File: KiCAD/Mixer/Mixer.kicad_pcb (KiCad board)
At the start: 2 copper layers, 30 x 118.5 mm, 63 parts, among them J1 AudioJack2, J2 Conn_02x05_Odd_Even, J3 Conn_02x03_Odd_Even, J4 Conn_02x08_Odd_Even, J5 AudioJack2, Q1 MMBFJ111, Q2 MMBFJ111, Q3 MMBFJ111, Q4 MMBFJ111, SW1 SW_MEC_5G, SW2 SW_MEC_5G, U1 NE5532, U2 NE5532, U3 NE5532, U4 NE5532, U5 NE5532, U6 NE5532

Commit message: überarbeitete Schaltung und PCB Desing...v1.0 FERTIG
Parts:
- removed C2: 100n, Capacitor_SMD:C_0805_2012Metric_Pad1.18x1.45mm_HandSolder
- removed D1, D2, D5, D6: D, Diode_SMD:D_SOD-123
- removed J2: Conn_02x05_Odd_Even, Connector_PinHeader_2.54mm:PinHeader_2x05_P2.54mm_Vertical
- removed J3: Conn_02x03_Odd_Even, Connector_PinHeader_2.54mm:PinHeader_2x03_P2.54mm_Vertical
- removed RV8: 100, Potentiometer_THT:Potentiometer_Alps_RK09K_Single_Vertical
- added C11: 100n, Capacitor_SMD:C_0805_2012Metric_Pad1.18x1.45mm_HandSolder, B.Cu at (146.3, 55.4)
- added C12: 100n, Capacitor_SMD:C_0805_2012Metric_Pad1.18x1.45mm_HandSolder, B.Cu at (146.3, 65.0)
- added C13: 100n, Capacitor_SMD:C_0805_2012Metric_Pad1.18x1.45mm_HandSolder, B.Cu at (130.9, 62.9)
- added C14: 100n, Capacitor_SMD:C_0805_2012Metric_Pad1.18x1.45mm_HandSolder, B.Cu at (130.9, 72.6)
- added C15: 100n, Capacitor_SMD:C_0805_2012Metric_Pad1.18x1.45mm_HandSolder, B.Cu at (146.3, 63.0)
- added C16: 100n, Capacitor_SMD:C_0805_2012Metric_Pad1.18x1.45mm_HandSolder, B.Cu at (146.3, 72.6)
- added C17: 100u, Capacitor_THT:CP_Radial_D5.0mm_P2.50mm, B.Cu at (138.6, 125.4)
- added C33: 100n, Capacitor_SMD:C_0805_2012Metric_Pad1.18x1.45mm_HandSolder, B.Cu at (129.7, 47.6)
- added C34: 100n, Capacitor_SMD:C_0805_2012Metric_Pad1.18x1.45mm_HandSolder, B.Cu at (139.7, 47.7)
- added C35: 100n, Capacitor_SMD:C_0805_2012Metric_Pad1.18x1.45mm_HandSolder, B.Cu at (137.5, 47.6)
- added C37: 100n, Capacitor_SMD:C_0805_2012Metric_Pad1.18x1.45mm_HandSolder, B.Cu at (147.3, 47.6)
- added C40: 100n, Capacitor_SMD:C_0805_2012Metric_Pad1.18x1.45mm_HandSolder, B.Cu at (138.8, 85.2)
- added C41: 100n, Capacitor_SMD:C_0805_2012Metric_Pad1.18x1.45mm_HandSolder, B.Cu at (138.8, 94.9)
- added D3: 1N5711, Diode_SMD:D_SMA, B.Cu at (133.5, 126.9)
- added D4: 1N5711, Diode_SMD:D_SMA, B.Cu at (143.7, 137.1)
- added J10: Conn_02x09_Odd_Even, Connector_PinHeader_2.54mm:PinHeader_2x09_P2.54mm_Vertical, B.Cu at (143.3, 99.0)
- added J11: Conn_02x09_Odd_Even, Connector_PinHeader_2.54mm:PinHeader_2x09_P2.54mm_Vertical, B.Cu at (136.4, 99.0)
- added J6: Conn_02x05_Odd_Even, Connector_PinHeader_2.54mm:PinHeader_2x05_P2.54mm_Vertical, B.Cu at (139.8, 128.9)
- added J7: Conn_01x02_Socket, Connector_PinHeader_2.54mm:PinHeader_1x02_P2.54mm_Vertical, F.Cu at (146.0, 33.6)
- added J8: Conn_01x02_Socket, Connector_PinHeader_2.54mm:PinHeader_1x02_P2.54mm_Vertical, F.Cu at (135.3, 37.4)
- added J9: Conn_01x02_Socket, Connector_PinHeader_2.54mm:PinHeader_1x02_P2.54mm_Vertical, F.Cu at (146.0, 37.3)
- added R25: 1k, Resistor_SMD:R_0805_2012Metric_Pad1.20x1.40mm_HandSolder, B.Cu at (151.1, 59.3)
- added R26: 1k, Resistor_SMD:R_0805_2012Metric_Pad1.20x1.40mm_HandSolder, B.Cu at (141.6, 59.2)
- added R29: 1k, Resistor_SMD:R_0805_2012Metric_Pad1.20x1.40mm_HandSolder, B.Cu at (143.5, 80.2)
- added R30: 1k, Resistor_SMD:R_0805_2012Metric_Pad1.20x1.40mm_HandSolder, B.Cu at (134.0, 80.2)
- added R31: 1k, Resistor_SMD:R_0805_2012Metric_Pad1.20x1.40mm_HandSolder, B.Cu at (132.0, 84.0)
- added R32: 1k, Resistor_SMD:R_0805_2012Metric_Pad1.20x1.40mm_HandSolder, B.Cu at (132.0, 80.2)
- added R33: 1k, Resistor_SMD:R_0805_2012Metric_Pad1.20x1.40mm_HandSolder, B.Cu at (145.5, 80.2)
- added R34: 1k, Resistor_SMD:R_0805_2012Metric_Pad1.20x1.40mm_HandSolder, B.Cu at (145.5, 84.0)
- added R35: 1k, Resistor_SMD:R_0805_2012Metric_Pad1.20x1.40mm_HandSolder, B.Cu at (143.5, 84.0)
- added R36: 1k, Resistor_SMD:R_0805_2012Metric_Pad1.20x1.40mm_HandSolder, B.Cu at (134.0, 84.0)
- added R37: 1k, Resistor_SMD:R_0805_2012Metric_Pad1.20x1.40mm_HandSolder, B.Cu at (143.6, 91.2)
- added R38: 1k, Resistor_SMD:R_0805_2012Metric_Pad1.20x1.40mm_HandSolder, B.Cu at (134.0, 91.0)
- added R39: 1k, Resistor_SMD:R_0805_2012Metric_Pad1.20x1.40mm_HandSolder, B.Cu at (124.1, 59.2)
- added R40: 1k, Resistor_SMD:R_0805_2012Metric_Pad1.20x1.40mm_HandSolder, B.Cu at (139.6, 59.2)
- added R41: 1k, Resistor_SMD:R_0805_2012Metric_Pad1.20x1.40mm_HandSolder, B.Cu at (132.0, 91.0)
- added R42: 1k, Resistor_SMD:R_0805_2012Metric_Pad1.20x1.40mm_HandSolder, B.Cu at (145.6, 91.2)
- added R43: 1k, Resistor_SMD:R_0805_2012Metric_Pad1.20x1.40mm_HandSolder, B.Cu at (137.6, 59.2)
- added R44: 1k, Resistor_SMD:R_0805_2012Metric_Pad1.20x1.40mm_HandSolder, B.Cu at (153.1, 59.3)
- added R45: 1k, Resistor_SMD:R_0805_2012Metric_Pad1.20x1.40mm_HandSolder, B.Cu at (139.6, 68.8)
- added R46: 1k, Resistor_SMD:R_0805_2012Metric_Pad1.20x1.40mm_HandSolder, B.Cu at (153.1, 68.9)
- added R47: 1k, Resistor_SMD:R_0805_2012Metric_Pad1.20x1.40mm_HandSolder, B.Cu at (151.1, 68.9)
- added R48: 1k, Resistor_SMD:R_0805_2012Metric_Pad1.20x1.40mm_HandSolder, B.Cu at (141.6, 68.8)
- added R49: 1k, Resistor_SMD:R_0805_2012Metric_Pad1.20x1.40mm_HandSolder, B.Cu at (124.1, 68.8)
- added R50: 1k, Resistor_SMD:R_0805_2012Metric_Pad1.20x1.40mm_HandSolder, B.Cu at (137.6, 68.8)
- added R51: 1k, Resistor_SMD:R_0805_2012Metric_Pad1.20x1.40mm_HandSolder, B.Cu at (135.6, 68.8)
- added R52: 1k, Resistor_SMD:R_0805_2012Metric_Pad1.20x1.40mm_HandSolder, B.Cu at (126.1, 68.8)
- added RV10: 1k, Potentiometer_THT:Potentiometer_Alps_RK09K_Single_Vertical, F.Cu at (118.4, 87.4)
- added RV11: 1k, Potentiometer_THT:Potentiometer_Alps_RK09K_Single_Vertical, F.Cu at (153.7, 71.8)
- added RV12: 1k, Potentiometer_THT:Potentiometer_Alps_RK09K_Single_Vertical, F.Cu at (153.7, 87.4)
- added U7: NE5532, Package_SO:SOIC-8_3.9x4.9mm_P1.27mm, B.Cu at (146.3, 59.2)
- added U8: NE5532, Package_SO:SOIC-8_3.9x4.9mm_P1.27mm, B.Cu at (146.3, 68.8)
- C1, C3: value 470u -> 4,7
- C4, C6: value 100n -> 220n
- C5: value 100n -> 100u; footprint Capacitor_SMD:C_0805_2012Metric_Pad1.18x1.45mm_HandSolder -> Capacitor_THT:CP_Radial_D5.0mm_P2.50mm
- J4: value Conn_02x08_Odd_Even -> Conn_01x02_Socket; footprint Connector_PinHeader_2.54mm:PinHeader_2x08_P2.54mm_Vertical -> Connector_PinHeader_2.54mm:PinHeader_1x02_P2.54mm_Vertical; moved to F.Cu
- R1, R13, R15, R3: value R -> 10k
- R11, R12: value 100 -> R
- R14, R2: value R -> 1k
- R23, R24, RV4: value 100 -> 1k
- moved C5 171.1 mm to (138.6, 145.0), turned to 90 degrees
- moved R12 147.1 mm to (160.4, 38.5), turned to -90 degrees
- moved R13 134.5 mm to (159.8, 57.8)
- moved R18 134.2 mm to (155.9, 129.9), turned to 180 degrees
- moved R16 133.7 mm to (155.9, 131.9), turned to 0 degrees
- moved J4 133.7 mm to (135.3, 33.6), turned to -90 degrees
- moved C3 132.9 mm to (162.5, 38.5), turned to -90 degrees
- moved R21 132.8 mm to (157.2, 100.4), turned to 0 degrees
- moved R22 132.6 mm to (157.2, 107.1), turned to 0 degrees
- moved J5 131.9 mm to (151.1, 35.5)
- moved R19 131.8 mm to (155.9, 127.9), turned to 0 degrees
- moved C9 131.5 mm to (138.7, 77.6), turned to 180 degrees
- moved RV7 131.4 mm to (153.7, 105.0)
- moved R17 130.4 mm to (155.9, 125.8), turned to 180 degrees
- moved SW2 130.4 mm to (159.4, 124.4)
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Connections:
- C10 pad 2: +12V -> /Channel/+12V
- C5 pad 2: +12V -> Net-(D4-K)
- C7 pad 2: +12V -> /Channel/+12V
- C8 pad 2: +12V -> /Channel/+12V
- C9 pad 2: +12V -> /Channel/+12V
- J4 pad 1: -12V -> Net-(J4-Pin_1)
- J4 pad 2: -12V -> /Channel/Gain/gain_out
- R1 pad 1: Net-(D1-K) -> Net-(J4-Pin_1)
- R10 pad 2: /Channel/Main Mix/main_inR -> /Channel/Ch1_outR
- R11 pad 1: /Channel/Main Mix/main_inL -> GND
- R11 pad 2: Net-(U3A-+) -> /Channel/Gain/gain_in
- R12 pad 1: /Channel/Main Mix/main_inR -> GND
- R12 pad 2: Net-(U3B-+) -> /Channel/Gain1/gain_in
- R2 pad 2: Net-(D1-K) -> Net-(J4-Pin_1)
- R21 pad 2: /Channel/Main Mix1/main_inL -> /Channel/Ch2_outL
- R22 pad 2: /Channel/Main Mix1/main_inR -> /Channel/Ch2_outR
- R23 pad 1: /Channel/Main Mix1/main_inL -> Net-(U3B--)
- R23 pad 2: Net-(U5A-+) -> Net-(R23-Pad2)
- R24 pad 1: /Channel/Main Mix1/main_inR -> Net-(U3A--)
- R24 pad 2: Net-(U5B-+) -> Net-(R24-Pad2)
- R9 pad 2: /Channel/Main Mix/main_inL -> /Channel/Ch1_outL
- RV4 pad 1: Net-(U3A--) -> /Channel/Ch1_outL
- RV4 pad 2: /Channel/ch1send_L -> Net-(U3A--)
- RV4 pad 3: /Channel/ch1send_L -> Net-(U3A--)
- SW1 pad 1: -12V -> /Channel/-12V
- SW1 pad 2: -12V -> /Channel/-12V
- SW2 pad 1: -12V -> /Channel/-12V
- SW2 pad 2: -12V -> /Channel/-12V
- U1 pad 2: Net-(D1-K) -> Net-(J4-Pin_1)
- U1 pad 4: -12V -> /Channel/-12V
- U1 pad 8: +12V -> /Channel/+12V
- U2 pad 4: -12V -> /Channel/-12V
- U2 pad 8: +12V -> /Channel/+12V
- U3 pad 1: /Channel/ch1send_L -> Net-(R24-Pad2)
- U3 pad 3: Net-(U3A-+) -> GND
- U3 pad 4: -12V -> /Channel/-12V
- U3 pad 5: Net-(U3B-+) -> GND
- U3 pad 7: /Channel/ch1send_R -> Net-(R23-Pad2)
- U3 pad 8: +12V -> /Channel/+12V
- U4 pad 1: /Channel/ch1out_L -> Net-(R29-Pad2)
- U4 pad 2: /Channel/ch1out_L -> Net-(U4A--)
- U4 pad 3: /Channel/Main Mix/main_inL -> GND
- U4 pad 4: -12V -> /Channel/-12V
- U4 pad 5: /Channel/Main Mix/main_inR -> GND
- U4 pad 6: /Channel/ch1out_R -> Net-(U4B--)
- U4 pad 7: /Channel/ch1out_R -> Net-(R30-Pad2)
- U4 pad 8: +12V -> /Channel/+12V
- U5 pad 1: /Channel/ch1send_L -> /Channel/main_mixL
- U5 pad 3: Net-(U5A-+) -> GND
- U5 pad 4: -12V -> /Channel/-12V
- U5 pad 5: Net-(U5B-+) -> GND
- U5 pad 7: /Channel/ch1send_R -> /Channel/main_mixR
- U5 pad 8: +12V -> /Channel/+12V
- U6 pad 1: /Channel/ch1out_L -> /Channel/send_out1L
- U6 pad 2: /Channel/ch1out_L -> Net-(U6A--)
- U6 pad 3: /Channel/Main Mix1/main_inL -> GND
- U6 pad 4: -12V -> /Channel/-12V
- U6 pad 5: /Channel/Main Mix1/main_inR -> GND
- U6 pad 6: /Channel/ch1out_R -> Net-(U6B--)
- U6 pad 7: /Channel/ch1out_R -> /Channel/send_out1R
- U6 pad 8: +12V -> /Channel/+12V
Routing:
- net /Channel/-12V: track 0.00 -> 224.4 mm, vias 0 -> 10
- net /Channel/+12V: track 0.00 -> 143.8 mm, vias 0 -> 9
- net /Channel/Gain1/gain_out: track 0.00 -> 112.7 mm, vias 0 -> 2
- net /Channel/Gain/gain_out: track 0.00 -> 112.2 mm, vias 0 -> 5
- net /Channel/Fader/fader_out: track 0.00 -> 109.7 mm, vias 0 -> 1
- net GND: track 0.00 -> 104.5 mm, vias 0 -> 160
- net /Channel/Fader1/fader_out: track 0.00 -> 101.5 mm, vias 0 -> 1
- net /Channel/Ch1_outL: track 0.00 -> 80.1 mm, vias 0 -> 4
- net Net-(U1B--): track 0.00 -> 79.8 mm, vias 0 -> 2
- net Net-(U2B--): track 0.00 -> 78.0 mm, vias 0 -> 2
- net /Channel/pre_send2L: track 0.00 -> 75.8 mm, vias 0 -> 3
- net /Channel/pre_send2R: track 0.00 -> 72.3 mm, vias 0 -> 4
- net /Channel/pre_send1R: track 0.00 -> 68.0 mm, vias 0 -> 1
- net /Channel/Ch2_outL: track 0.00 -> 64.0 mm
- net /Channel/send_out2R: track 0.00 -> 62.1 mm, vias 0 -> 4
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- added copper zone on B.Cu, net GND
- added copper zone on F.Cu, net GND
- added copper zone on In1.Cu, net GND
- added copper zone on In2.Cu, net GND
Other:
- board size 30 x 118.5 mm -> 54 x 120 mm
- copper layers 2 -> 4

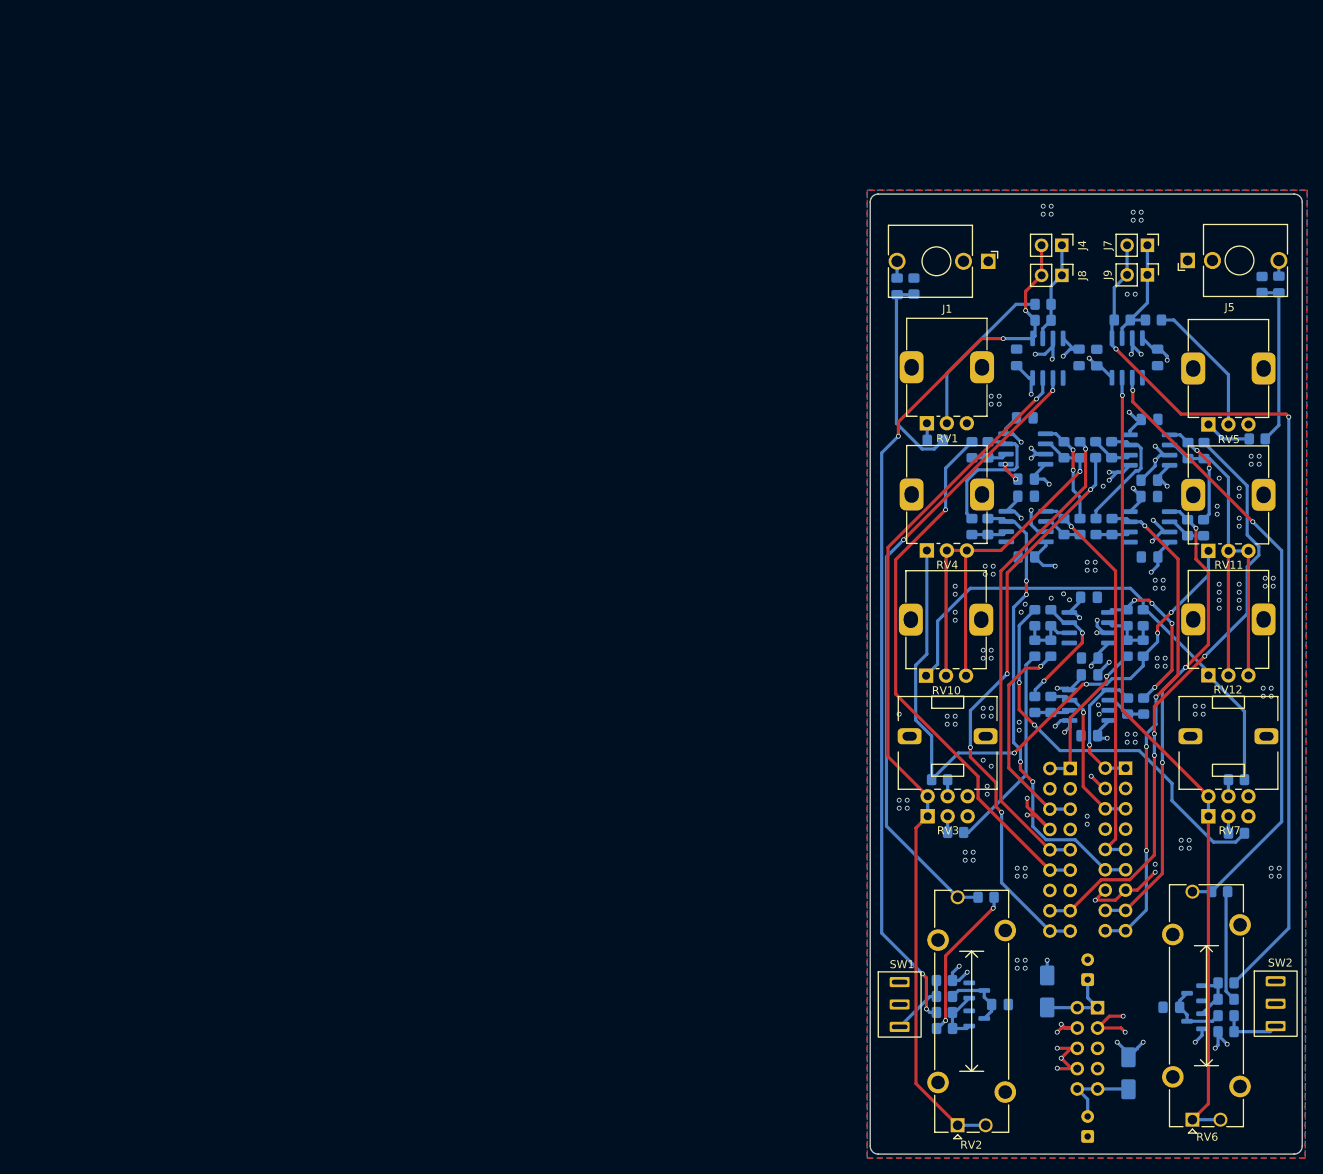
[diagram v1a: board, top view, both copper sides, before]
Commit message: Rework of schematic, with error fixes and reworked pcb
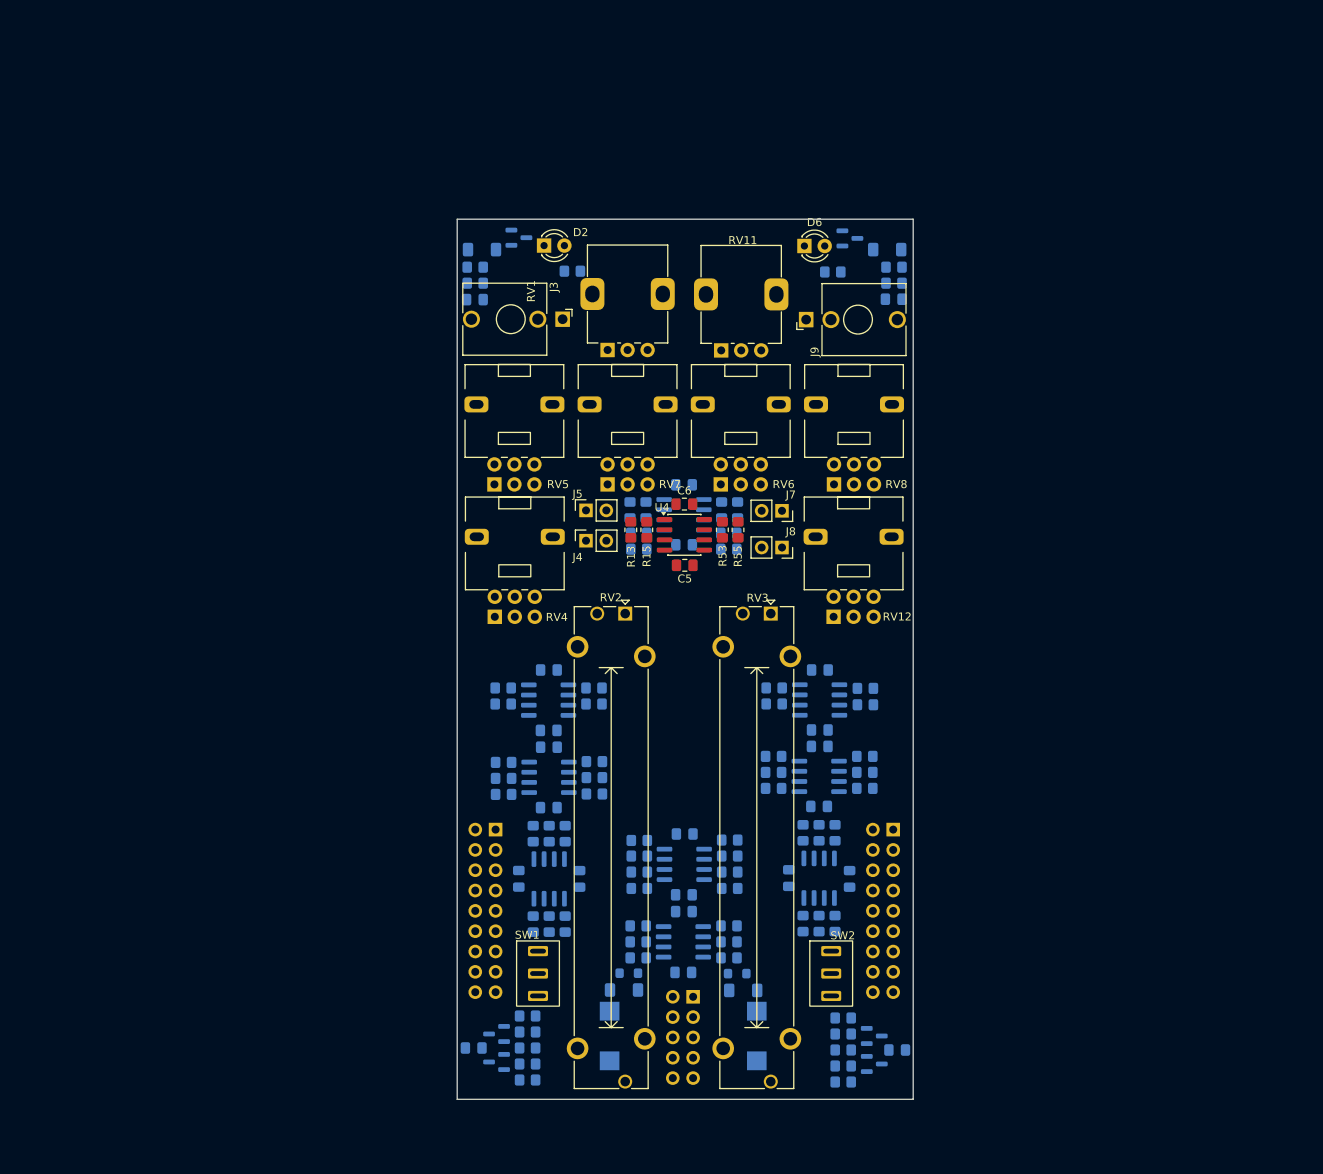
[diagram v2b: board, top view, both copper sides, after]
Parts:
- removed C33, C34, C35, C37, C40, C41: 100n, Capacitor_SMD:C_0805_2012Metric_Pad1.18x1.45mm_HandSolder
- removed J10, J11: Conn_02x09_Odd_Even, Connector_PinHeader_2.54mm:PinHeader_2x09_P2.54mm_Vertical
- removed R14: 1k, Resistor_SMD:R_0805_2012Metric_Pad1.20x1.40mm_HandSolder
- removed R16: 10k, Resistor_SMD:R_0805_2012Metric_Pad1.20x1.40mm_HandSolder
- removed R17, R5: 2k2, Resistor_SMD:R_0805_2012Metric_Pad1.20x1.40mm_HandSolder
- removed R18: 100k, Resistor_SMD:R_0805_2012Metric_Pad1.20x1.40mm_HandSolder
- removed RV10: 1k, Potentiometer_THT:Potentiometer_Alps_RK09K_Single_Vertical
- removed U5: NE5532, Package_SO:SOIC-8_3.9x4.9mm_P1.27mm
- added C18: 220n, Capacitor_SMD:C_0805_2012Metric_Pad1.18x1.45mm_HandSolder, B.Cu at (61.8, 134.0)
- added C19: 100u, 2917_Tantal_Elko:CAPPM7343X310N, B.Cu at (97.2, 132.5)
- added C2: 100n, Capacitor_SMD:C_0805_2012Metric_Pad1.18x1.45mm_HandSolder, B.Cu at (88.1, 63.6)
- added C20: 100u, 2917_Tantal_Elko:CAPPM7343X310N, B.Cu at (78.8, 132.5)
- added C21: 2u, Capacitor_SMD:C_0805_2012Metric_Pad1.18x1.45mm_HandSolder, B.Cu at (114.3, 40.4)
- added C22: 220n, Capacitor_SMD:C_0805_2012Metric_Pad1.18x1.45mm_HandSolder, B.Cu at (114.8, 134.2)
- added C25: 100n, Capacitor_SMD:C_0805_2012Metric_Pad1.18x1.45mm_HandSolder, B.Cu at (105.1, 86.7)
- added C26: 100n, Capacitor_SMD:C_0805_2012Metric_Pad1.18x1.45mm_HandSolder, B.Cu at (105.1, 94.2)
- added C27: 100n, Capacitor_SMD:C_0805_2012Metric_Pad1.18x1.45mm_HandSolder, B.Cu at (105.0, 103.8)
- added C28: 100n, Capacitor_SMD:C_0805_2012Metric_Pad1.18x1.45mm_HandSolder, B.Cu at (105.1, 96.3)
- added D1: 1N4148, Diode_SMD:D_MiniMELF, B.Cu at (62.9, 34.2)
- added D2: LED, LED_THT:LED_D3.0mm, F.Cu at (70.6, 33.7)
- added D5: 1N4148, Diode_SMD:D_MiniMELF, B.Cu at (113.5, 34.2)
- added D6: LED, LED_THT:LED_D3.0mm, F.Cu at (103.2, 33.7)
- added FB1: FerriteBead, Inductor_SMD:L_0805_2012Metric_Pad1.05x1.20mm_HandSolder, B.Cu at (94.8, 124.7)
- added FB2: FerriteBead, Inductor_SMD:L_0805_2012Metric_Pad1.05x1.20mm_HandSolder, B.Cu at (81.2, 124.6)
- added J2: Conn_02x09_Odd_Even, Connector_PinHeader_2.54mm:PinHeader_2x09_P2.54mm_Vertical, B.Cu at (114.2, 106.7)
- added J3: AudioJack2, Connector_Audio:Jack_3.5mm_QingPu_WQP-PJ398SM_Vertical_CircularHoles, F.Cu at (72.9, 42.9)
- added Q5: MMBFJ111, Package_TO_SOT_SMD:SOT-23, B.Cu at (111.9, 136.0)
- added Q6: MMBFJ111, Package_TO_SOT_SMD:SOT-23, B.Cu at (111.9, 132.5)
- added R27: 1k, Resistor_SMD:R_0805_2012Metric_Pad1.20x1.40mm_HandSolder, B.Cu at (65.5, 98.3)
- added R28: 1k, Resistor_SMD:R_0805_2012Metric_Pad1.20x1.40mm_HandSolder, B.Cu at (76.9, 98.2)
- added R53: 10k, Resistor_SMD:R_0805_2012Metric_Pad1.20x1.40mm_HandSolder, F.Cu at (92.9, 69.2)
- added R55: 0R, Resistor_SMD:R_0805_2012Metric_Pad1.20x1.40mm_HandSolder, F.Cu at (94.8, 69.2)
- added R57: 10K, Resistor_SMD:R_0805_2012Metric_Pad1.20x1.40mm_HandSolder, B.Cu at (92.8, 66.7)
- added R58: 10k, Resistor_SMD:R_0805_2012Metric_Pad1.20x1.40mm_HandSolder, B.Cu at (82.5, 69.6)
- added R59: 8k6, Resistor_SMD:R_0805_2012Metric_Pad1.20x1.40mm_HandSolder, B.Cu at (94.8, 66.7)
- added R60: 0R, Resistor_SMD:R_0805_2012Metric_Pad1.20x1.40mm_HandSolder, B.Cu at (93.7, 71.6)
- added R61: 5k, Resistor_SMD:R_0805_2012Metric_Pad1.20x1.40mm_HandSolder, B.Cu at (114.3, 38.4)
- added R62: 100k, Resistor_SMD:R_0805_2012Metric_Pad1.20x1.40mm_HandSolder, B.Cu at (114.3, 36.4)
- added R63: 4,7k, Resistor_SMD:R_0805_2012Metric_Pad1.20x1.40mm_HandSolder, B.Cu at (106.7, 37.0)
- added R64: 10k, Resistor_SMD:R_0805_2012Metric_Pad1.20x1.40mm_HandSolder, B.Cu at (108.0, 136.2)
- added R65: 2k2, Resistor_SMD:R_0805_2012Metric_Pad1.20x1.40mm_HandSolder, B.Cu at (108.0, 134.2)
- added R66: 100k, Resistor_SMD:R_0805_2012Metric_Pad1.20x1.40mm_HandSolder, B.Cu at (108.0, 138.2)
- added R67: 2k2, Resistor_SMD:R_0805_2012Metric_Pad1.20x1.40mm_HandSolder, B.Cu at (108.0, 132.2)
- added R68: 0R, Resistor_SMD:R_0805_2012Metric_Pad1.20x1.40mm_HandSolder, B.Cu at (108.0, 130.2)
- added R79: 10k, Resistor_SMD:R_0805_2012Metric_Pad1.20x1.40mm_HandSolder, B.Cu at (93.7, 69.6)
- added R80: 1k, Resistor_SMD:R_0805_2012Metric_Pad1.20x1.40mm_HandSolder, B.Cu at (71.2, 107.2)
- added R81: 1k, Resistor_SMD:R_0805_2012Metric_Pad1.20x1.40mm_HandSolder, B.Cu at (105.0, 107.1)
- added R82: 3k3, Resistor_SMD:R_0805_2012Metric_Pad1.20x1.40mm_HandSolder, B.Cu at (69.2, 107.2)
- added R83: 3k3, Resistor_SMD:R_0805_2012Metric_Pad1.20x1.40mm_HandSolder, B.Cu at (107.0, 107.1)
- added R84: 1k, Resistor_SMD:R_0805_2012Metric_Pad1.20x1.40mm_HandSolder, B.Cu at (71.2, 118.5)
- added R85: 1k, Resistor_SMD:R_0805_2012Metric_Pad1.20x1.40mm_HandSolder, B.Cu at (105.0, 118.4)
- added R86: 3k3, Resistor_SMD:R_0805_2012Metric_Pad1.20x1.40mm_HandSolder, B.Cu at (69.2, 118.5)
- added R87: 3k3, Resistor_SMD:R_0805_2012Metric_Pad1.20x1.40mm_HandSolder, B.Cu at (103.0, 118.4)
- added R88: 3k3, Resistor_SMD:R_0805_2012Metric_Pad1.20x1.40mm_HandSolder, B.Cu at (73.2, 118.5)
- added R89: 3k3, Resistor_SMD:R_0805_2012Metric_Pad1.20x1.40mm_HandSolder, B.Cu at (107.0, 118.4)
- added R90: 3k3, Resistor_SMD:R_0805_2012Metric_Pad1.20x1.40mm_HandSolder, B.Cu at (73.2, 107.2)
- added R91: 3k3, Resistor_SMD:R_0805_2012Metric_Pad1.20x1.40mm_HandSolder, B.Cu at (103.0, 107.1)
- added RV8: 1k, Potentiometer_THT:Potentiometer_Alps_RK09L_Double_Vertical, F.Cu at (106.8, 63.5)
- added U10: NE5532, Package_SO:SOIC-8_3.9x4.9mm_P1.27mm, B.Cu at (105.0, 90.5)
- added U11: NE5532, Package_SO:SOIC-8_3.9x4.9mm_P1.27mm, B.Cu at (105.0, 100.0)
- added U9: NE5532, Package_SO:SOIC-8_3.9x4.9mm_P1.27mm, B.Cu at (71.2, 100.1)
- C1, C3: value 4,7 -> 100n
- C17: value 100u -> 2u; footprint Capacitor_THT:CP_Radial_D5.0mm_P2.50mm -> Capacitor_SMD:C_0805_2012Metric_Pad1.18x1.45mm_HandSolder
- C4: value 220n -> 100n
- C5: value 100u -> 100n; footprint Capacitor_THT:CP_Radial_D5.0mm_P2.50mm -> Capacitor_SMD:C_0805_2012Metric_Pad1.18x1.45mm_HandSolder; moved to F.Cu
- C6: value 220n -> 100n; moved to F.Cu
- D3, D4: footprint Diode_SMD:D_SMA -> Diode_SMD:D_MiniMELF
- J1: value AudioJack2 -> Conn_02x09_Odd_Even; footprint Connector_Audio:Jack_3.5mm_QingPu_WQP-PJ398SM_Vertical_CircularHoles -> Connector_PinHeader_2.54mm:PinHeader_2x09_P2.54mm_Vertical; moved to B.Cu
- J4, J7, J8: footprint Connector_PinHeader_2.54mm:PinHeader_1x02_P2.54mm_Vertical -> Connector_PinSocket_2.54mm:PinSocket_1x02_P2.54mm_Vertical
- J5: value AudioJack2 -> Conn_01x02_Socket; footprint Connector_Audio:Jack_3.5mm_QingPu_WQP-PJ398SM_Vertical_CircularHoles -> Connector_PinSocket_2.54mm:PinSocket_1x02_P2.54mm_Vertical
- J9: value Conn_01x02_Socket -> AudioJack2; footprint Connector_PinHeader_2.54mm:PinHeader_1x02_P2.54mm_Vertical -> Connector_Audio:Jack_3.5mm_QingPu_WQP-PJ398SM_Vertical_CircularHoles
- Q1, Q4: value MMBFJ111 -> NPN
- R1: value 10k -> 5k
- R10: value R -> 100k
- R11, R9: value R -> 2k2
- R12: value R -> 0R
- R13, U4: moved to F.Cu
- R15: value 10k -> 0R; moved to F.Cu
- R19: value 2k2 -> 1k
- R2: value 1k -> 100k
- R21, R22: value R -> 1k
- R3: value 10k -> 4,7k
- R35, R36, R37, R38, R51, R52: value 1k -> 0R
- R4: value 1k -> 10K
- R6: value 2k2 -> 8k6
- R7: value 100k -> 0R
- RV1: value 10k -> 100K
- RV11: value 1k -> 100K
- RV12, RV4: value 1k -> 10k; footprint Potentiometer_THT:Potentiometer_Alps_RK09K_Single_Vertical -> Potentiometer_THT:Potentiometer_Alps_RK09L_Double_Vertical
- RV2: value 1k -> R_Potentiometer; footprint Potentiometer_THT:Potentiometer_Bourns_PTA1543_Single_Slide -> Potentiometer_THT:Potentiometer_Bourns_PTA4543_Single_Slide
- RV3: value 10k -> R_Potentiometer; footprint Potentiometer_THT:Potentiometer_Alps_RK09L_Double_Vertical -> Potentiometer_THT:Potentiometer_Bourns_PTA4543_Single_Slide
- RV5: value 10k -> 1k; footprint Potentiometer_THT:Potentiometer_Alps_RK09K_Single_Vertical -> Potentiometer_THT:Potentiometer_Alps_RK09L_Double_Vertical
- RV6: footprint Potentiometer_THT:Potentiometer_Bourns_PTA1543_Single_Slide -> Potentiometer_THT:Potentiometer_Alps_RK09L_Double_Vertical
- RV7: value 10k -> 1k
- moved R12 129.6 mm to (68.5, 130.0), turned to 180 degrees
- moved C17 114.4 mm to (62.0, 40.4), turned to 0 degrees
- moved Q1 113.1 mm to (67.5, 32.7)
- moved R11 106.8 mm to (68.5, 134.0), turned to 0 degrees
- moved C3 106.5 mm to (88.1, 114.8), turned to 0 degrees
- moved Q4 103.7 mm to (108.8, 32.8), turned to 0 degrees
- moved RV6 98.9 mm to (92.7, 63.5)
- moved R19 98.4 mm to (65.5, 89.0)
- moved U2 97.3 mm to (71.2, 112.8)
- moved J1 94.0 mm to (64.5, 106.7), turned to 180 degrees
- moved RV5 89.6 mm to (64.4, 63.5)
- moved C6 87.5 mm to (88.2, 66.0), turned to 0 degrees
- moved Q3 87.4 mm to (64.7, 135.7)
- moved C5 87.4 mm to (88.2, 73.6), turned to 180 degrees
- moved RV7 85.8 mm to (78.5, 63.5)
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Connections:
- C1 pad 1: Net-(C1-Pad1) -> GND
- C1 pad 2: /Channel/Gain/gain_in -> /Channel/+12V
- C10 pad 2: /Channel/+12V -> Net-(U10C-V+)
- C12 pad 2: /Channel/+12V -> /Channel/-12V
- C13 pad 2: /Channel/-12V -> /Channel/+12V
- C15 pad 2: /Channel/-12V -> /Channel/+12V
- C17 pad 1: Net-(D3-A) -> Net-(C17-Pad1)
- C17 pad 2: GND -> /Channel/Gain/gain_in
- C3 pad 1: Net-(C3-Pad1) -> GND
- C3 pad 2: /Channel/Gain1/gain_in -> /Channel/+12V
- C4 pad 1: Net-(Q1-G) -> GND
- C4 pad 2: GND -> /Channel/-12V
- C5 pad 2: Net-(D4-K) -> /Channel/+12V
- C6 pad 1: Net-(Q3-G) -> GND
- C6 pad 2: GND -> /Channel/-12V
- C8 pad 2: /Channel/+12V -> /Channel/-12V
- C9 pad 2: /Channel/+12V -> Net-(U10C-V-)
- D3 pad 1: /Channel/+12V -> Net-(D3-K)
- D4 pad 2: /Channel/-12V -> Net-(D4-A)
- J4 pad 2: /Channel/Gain/gain_out -> Net-(J4-Pin_2)
- J7 pad 2: /Channel/Gain1/gain_out -> Net-(J7-Pin_2)
- J8 pad 1: Net-(J4-Pin_1) -> Net-(J7-Pin_1)
- J8 pad 2: /Channel/Gain/gain_out -> Net-(J7-Pin_2)
- Q1 pad 1: Net-(Q1-D) -> Net-(D2-K)
- Q1 pad 2: GND -> Net-(D1-K)
- Q1 pad 3: Net-(Q1-G) -> GND
- Q2 pad 1: Net-(Q1-D) -> Net-(Q2-D)
- Q2 pad 3: Net-(Q1-G) -> Net-(Q2-G)
- Q3 pad 1: Net-(Q3-D) -> Net-(Q2-D)
- Q3 pad 3: Net-(Q3-G) -> Net-(Q2-G)
- Q4 pad 1: Net-(Q3-D) -> Net-(D6-K)
- Q4 pad 2: GND -> Net-(D5-K)
- Q4 pad 3: Net-(Q3-G) -> GND
- R1 pad 1: Net-(J4-Pin_1) -> GND
- R1 pad 2: /Channel/Gain/gain_out -> /Channel/Gain/gain_in
- R10 pad 2: /Channel/Ch1_outR -> Net-(Q2-G)
- R11 pad 1: GND -> Net-(Q2-D)
- R11 pad 2: /Channel/Gain/gain_in -> Net-(R11-Pad2)
- R12 pad 1: GND -> /Channel/Fader/fader_in
- R12 pad 2: /Channel/Gain1/gain_in -> Net-(R11-Pad2)
- R13 pad 1: /Channel/Gain1/gain_in -> /Channel/Fader/fader_in
- R13 pad 2: Net-(R13-Pad2) -> Net-(U4A--)
- R15 pad 1: Net-(J7-Pin_1) -> /Channel/Fader/fader_out
- R15 pad 2: /Channel/Gain1/gain_out -> Net-(R15-Pad2)
- R19 pad 1: Net-(Q3-D) -> /Channel/pre_send1L
- R19 pad 2: /Channel/Fader1/fader_in -> Net-(U8A--)
- R2 pad 1: Net-(R2-Pad1) -> /Channel/Gain/gain_in
- R2 pad 2: Net-(J4-Pin_1) -> Net-(D1-K)
- R20 pad 1: /Channel/Fader1/fader_in -> /Channel/pre_send1R
- R20 pad 2: Net-(U2B--) -> Net-(U8B--)
- R21 pad 1: Net-(R21-Pad1) -> /Channel/pre_send2L
- R21 pad 2: /Channel/Ch2_outL -> Net-(U10A--)
- R22 pad 1: Net-(R22-Pad1) -> /Channel/pre_send2R
- R22 pad 2: /Channel/Ch2_outR -> Net-(U10B--)
- R23 pad 1: Net-(U3B--) -> Net-(U8A--)
- R24 pad 1: Net-(U3A--) -> Net-(U8B--)
- R25 pad 1: Net-(U7A--) -> Net-(U10A--)
- R26 pad 1: Net-(U7B--) -> Net-(U10B--)
- R29 pad 1: Net-(U4A--) -> Net-(R25-Pad2)
- R29 pad 2: Net-(R29-Pad2) -> Net-(U11A--)
- R3 pad 1: /Channel/Gain/gain_in -> /Channel/+12V
- R3 pad 2: Net-(R3-Pad2) -> Net-(D2-A)
- R30 pad 1: Net-(U4B--) -> Net-(R26-Pad2)
- R30 pad 2: Net-(R30-Pad2) -> Net-(U11B--)
- R31 pad 1: /Channel/Ch1_outR -> Net-(U9B--)
- R31 pad 2: Net-(U4B--) -> Net-(R31-Pad2)
- R32 pad 1: /Channel/Ch2_outR -> Net-(U9A--)
- R32 pad 2: Net-(U4B--) -> Net-(R32-Pad2)
- R33 pad 1: /Channel/Ch2_outL -> Net-(U11A--)
- R33 pad 2: Net-(U4A--) -> Net-(R33-Pad2)
- R34 pad 1: /Channel/Ch1_outL -> Net-(U11B--)
- R34 pad 2: Net-(U4A--) -> Net-(R34-Pad2)
- R35 pad 1: /Channel/pre_mixL -> /Channel/send_out1L
- R35 pad 2: Net-(U4A--) -> Net-(R32-Pad2)
- R36 pad 1: /Channel/pre_mixR -> /Channel/send_out1R
- R36 pad 2: Net-(U4B--) -> Net-(R31-Pad2)
- R37 pad 1: Net-(U5A--) -> /Channel/send_out2L
- R37 pad 2: /Channel/main_mixL -> Net-(R33-Pad2)
- R38 pad 1: Net-(U5B--) -> /Channel/send_out2R
- R38 pad 2: /Channel/main_mixR -> Net-(R34-Pad2)
- R39 pad 1: /Channel/pre_send1R -> /Channel/pre_mixL
- R39 pad 2: Net-(U3B--) -> Net-(U6A--)
- R4 pad 1: /Channel/Fader/fader_in -> /Channel/Gain/gain_in
- R4 pad 2: Net-(U1B--) -> Net-(U1A--)
- R40 pad 1: /Channel/pre_send2R -> /Channel/Ch1_outL
- R40 pad 2: Net-(U7B--) -> Net-(U6A--)
- R41 pad 1: Net-(R30-Pad2) -> /Channel/Ch2_outL
- R41 pad 2: Net-(U5B--) -> Net-(U6A--)
- R42 pad 1: Net-(R29-Pad2) -> /Channel/Ch1_outR
- R42 pad 2: Net-(U5A--) -> Net-(U6B--)
- R43 pad 1: /Channel/pre_send1L -> /Channel/Ch2_outR
- R43 pad 2: Net-(U3A--) -> Net-(U6B--)
- R44 pad 1: /Channel/pre_send2L -> /Channel/pre_mixR
- R44 pad 2: Net-(U7A--) -> Net-(U6B--)
- R45 pad 1: Net-(R26-Pad2) -> Net-(U6A--)
- R45 pad 2: Net-(U8B--) -> Net-(R45-Pad2)
- R46 pad 1: Net-(R25-Pad2) -> Net-(U6B--)
- R46 pad 2: Net-(U8A--) -> Net-(R46-Pad2)
- R47 pad 1: Net-(U8A--) -> Net-(R45-Pad2)
- R47 pad 2: /Channel/send_out2L -> Net-(U7A--)
- R48 pad 1: Net-(U8B--) -> Net-(R46-Pad2)
- R48 pad 2: /Channel/send_out2R -> Net-(U7B--)
- R49 pad 1: Net-(R23-Pad2) -> Net-(U7A--)
- R49 pad 2: Net-(U6B--) -> Net-(R49-Pad2)
- R50 pad 1: Net-(R24-Pad2) -> Net-(U7B--)
- R50 pad 2: Net-(U6A--) -> Net-(R50-Pad2)
- R51 pad 1: Net-(U6A--) -> /Channel/main_mixL
- R51 pad 2: /Channel/send_out1L -> Net-(R49-Pad2)
- R52 pad 1: Net-(U6B--) -> /Channel/main_mixR
- R52 pad 2: /Channel/send_out1R -> Net-(R50-Pad2)
- R6 pad 1: Net-(Q1-D) -> Net-(U1A--)
- R6 pad 2: /Channel/Fader/fader_in -> Net-(J4-Pin_1)
- R7 pad 1: Net-(R7-Pad1) -> /Channel/Gain/gain_out
- R7 pad 2: Net-(Q1-G) -> Net-(J4-Pin_2)
- R8 pad 2: Net-(R7-Pad1) -> Net-(R10-Pad1)
- R9 pad 1: Net-(R9-Pad1) -> /Channel/Gain/gain_out
- R9 pad 2: /Channel/Ch1_outL -> Net-(Q2-D)
- RV1 pad 1: Net-(R3-Pad2) -> Net-(R58-Pad2)
- RV1 pad 2: Net-(R2-Pad1) -> Net-(U1A--)
- RV11 pad 1: /Channel/Ch1_outL -> Net-(R79-Pad2)
- RV11 pad 2: Net-(U7A--) -> Net-(U1B--)
- RV11 pad 3: Net-(U7A--) -> GND
- RV12 pad 1: /Channel/Ch2_outL -> /Channel/Fader1/fader_in
- RV12 pad 2: Net-(U7A--) -> Net-(U3B-+)
- RV12 pad 3: Net-(U7A--) -> GND
- RV2 pad 1: /Channel/Fader/fader_out -> Net-(R15-Pad2)
- RV2 pad 2: /Channel/Fader/fader_out -> Net-(R15-Pad2)
- RV2 pad 3: Net-(U1B--) -> Net-(U4A--)
- RV3 pad 1: /Channel/Fader/fader_out -> Net-(R55-Pad2)
- RV3 pad 2: Net-(R10-Pad1) -> Net-(R55-Pad2)
- RV3 pad 3: GND -> Net-(U4B--)
- RV4 pad 1: /Channel/Ch1_outL -> /Channel/Fader/fader_out
- RV4 pad 2: Net-(U3A--) -> Net-(U2B-+)
- RV4 pad 3: Net-(U3A--) -> GND
- RV5 pad 1: Net-(R13-Pad2) -> /Channel/Ch1_outL
- RV5 pad 2: Net-(R14-Pad1) -> Net-(U8A--)
- RV5 pad 3: GND -> Net-(U8A--)
- RV6 pad 1: /Channel/Fader1/fader_out -> /Channel/Ch2_outL
- RV6 pad 2: /Channel/Fader1/fader_out -> Net-(U8A--)
- RV6 pad 3: Net-(U2B--) -> Net-(U8A--)
- RV7 pad 1: /Channel/Fader1/fader_out -> /Channel/Ch1_outL
- RV7 pad 2: Net-(R22-Pad1) -> Net-(U10A--)
- RV7 pad 3: GND -> Net-(U10A--)
- RV7 pad 4: /Channel/Fader1/fader_out -> /Channel/Ch1_outR
- RV7 pad 5: Net-(R21-Pad1) -> Net-(U10B--)
- RV7 pad 6: GND -> Net-(U10B--)
- SW1 pad 3: Net-(R7-Pad1) -> Net-(R10-Pad1)
- U1 pad 1: /Channel/Gain/gain_out -> Net-(J4-Pin_2)
- U1 pad 2: Net-(J4-Pin_1) -> Net-(U1A--)
- U1 pad 7: /Channel/Fader/fader_out -> Net-(J7-Pin_2)
- U2 pad 1: /Channel/Gain1/gain_out -> /Channel/Pan/pan_outL
- U2 pad 2: Net-(J7-Pin_1) -> Net-(U2A--)
- U2 pad 3: GND -> Net-(U2A-+)
- U2 pad 5: GND -> Net-(U2B-+)
- U2 pad 7: /Channel/Fader1/fader_out -> /Channel/Pan/pan_outR
- U3 pad 1: Net-(R24-Pad2) -> /Channel/Pan1/pan_outL
- U3 pad 3: GND -> Net-(U3A-+)
- U3 pad 5: GND -> Net-(U3B-+)
- U3 pad 7: Net-(R23-Pad2) -> /Channel/Pan1/pan_outR
- U4 pad 1: Net-(R29-Pad2) -> Net-(R15-Pad2)
- U4 pad 4: /Channel/-12V -> /Channel/+12V
- U4 pad 7: Net-(R30-Pad2) -> Net-(R55-Pad2)
- U4 pad 8: /Channel/+12V -> /Channel/-12V
- U6 pad 1: /Channel/send_out1L -> Net-(R45-Pad2)
- U6 pad 7: /Channel/send_out1R -> Net-(R46-Pad2)
- U7 pad 1: Net-(R25-Pad2) -> Net-(R49-Pad2)
- U7 pad 7: Net-(R26-Pad2) -> Net-(R50-Pad2)
- U8 pad 1: /Channel/send_out2L -> Net-(R23-Pad2)
- U8 pad 4: /Channel/-12V -> /Channel/+12V
- U8 pad 7: /Channel/send_out2R -> Net-(R24-Pad2)
- U8 pad 8: /Channel/+12V -> /Channel/-12V
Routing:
- net /Channel/-12V: track 224.4 -> 0.00 mm, vias 10 -> 0
- net /Channel/+12V: track 143.8 -> 0.00 mm, vias 9 -> 0
- net /Channel/Gain1/gain_out: track 112.7 -> 0.00 mm, vias 2 -> 0
- net /Channel/Gain/gain_out: track 112.2 -> 0.00 mm, vias 5 -> 0
- net /Channel/Fader/fader_out: track 109.7 -> 0.00 mm, vias 1 -> 0
- net GND: track 104.5 -> 0.00 mm, vias 160 -> 0
- net /Channel/Fader1/fader_out: track 101.5 -> 0.00 mm, vias 1 -> 0
- net /Channel/Ch1_outL: track 80.1 -> 0.00 mm, vias 4 -> 0
- net Net-(U1B--): track 79.8 -> 0.00 mm, vias 2 -> 0
- net Net-(U2B--): track 78.0 -> 0.00 mm, vias 2 -> 0
- net /Channel/pre_send2L: track 75.8 -> 0.00 mm, vias 3 -> 0
- net /Channel/pre_send2R: track 72.3 -> 0.00 mm, vias 4 -> 0
- net /Channel/pre_send1R: track 68.0 -> 0.00 mm, vias 1 -> 0
- net /Channel/Ch2_outL: track 64.0 -> 0.00 mm
- net /Channel/send_out2R: track 62.1 -> 0.00 mm, vias 4 -> 0
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- removed copper zone on B.Cu, net GND
- removed copper zone on F.Cu, net GND
- removed copper zone on In1.Cu, net GND
- removed copper zone on In2.Cu, net GND
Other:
- board size 54 x 120 mm -> 57 x 110 mm
- board text added: "-12V"
